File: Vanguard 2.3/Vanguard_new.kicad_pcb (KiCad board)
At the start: 4 copper layers, 42.3 x 51.9 mm, 88 parts, among them J1 USB_C_Receptacle_USB2.0_16P, J2 Conn_02x03_Pin, J3 Micro_SD_Card_Det1, J4 STARBOARD_SERVO, J5 PORTSIDE_SERVO, J6 Battery In, J7 EJECTION_SERVO, Q1 BSS138, Q2 BSS138, Q3 BSS138, Q4 BSS138, U1 ATSAMD11D14A-M, U2 ATmega4809-A, U3 AT25DF641A-SH-T, U4 AP2112K-3.3, U5 BD1020HFV, U6 BNO086, U7 TXB0104D, U8 TPS61092, U9 MPM3610AGQV-P, Y1 32.768kHz

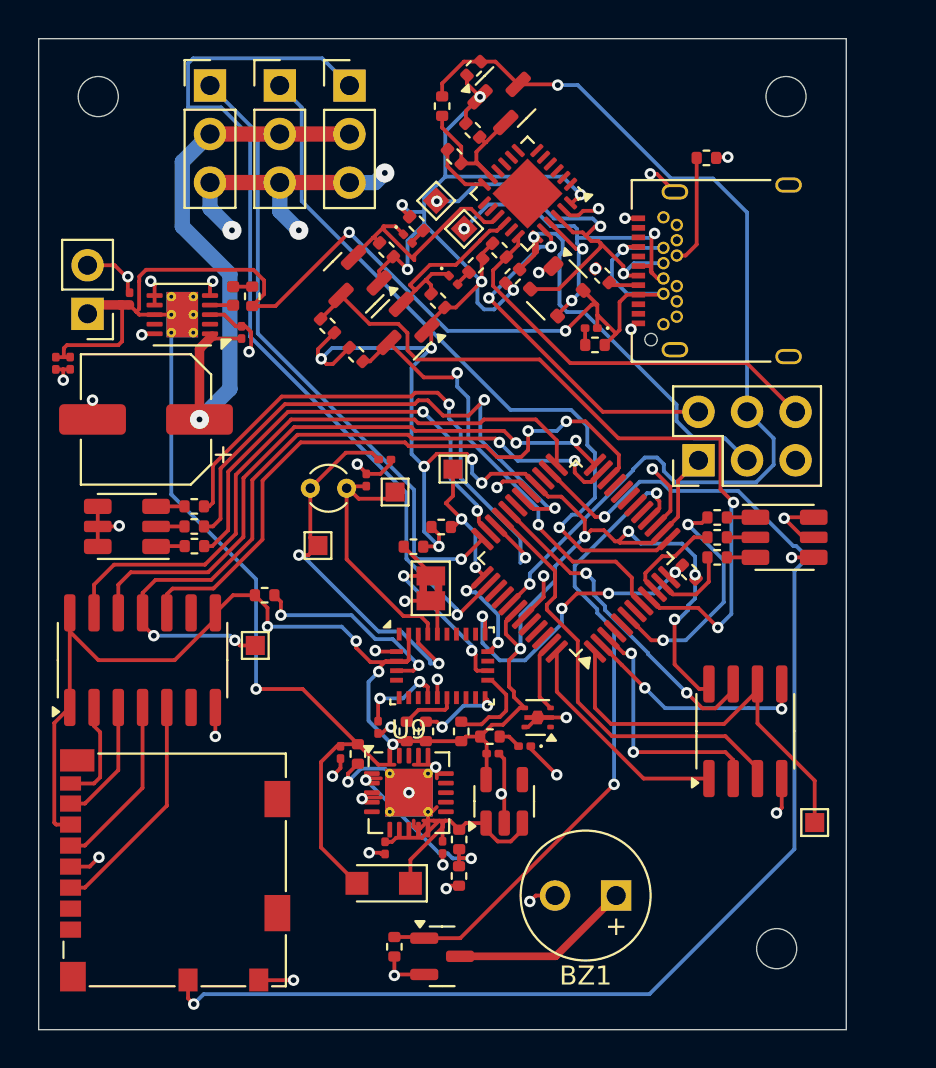
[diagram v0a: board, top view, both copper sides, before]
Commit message: wired u9 + new drc rules
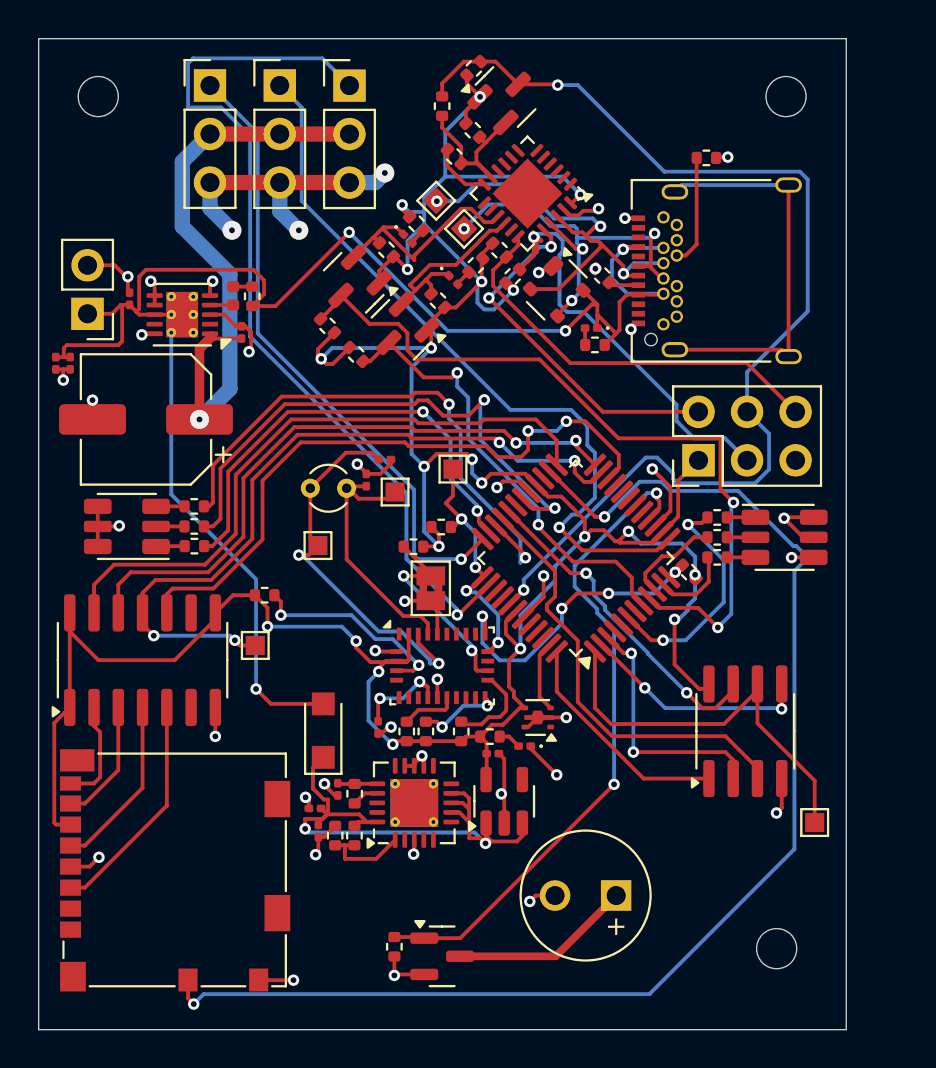
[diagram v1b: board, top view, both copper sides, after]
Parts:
- moved D6 8.59 mm to (107.3, 120.2), turned to 90 degrees
- moved C5 6.98 mm to (106.8, 124.3), turned to 180 degrees
- moved R16 6.82 mm to (107.9, 125.7), turned to 90 degrees
- moved R15 5.49 mm to (108.9, 125.7)
- moved C11 3.60 mm to (107.0, 125.4)
- moved R14 2.09 mm to (108.9, 123.5)
- moved C4 1.94 mm to (108.0, 123.3)
- moved U9 0.61 mm to (112.0, 124.0), turned to 90 degrees
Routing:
- net unconnected-(J1-SHIELD-PadS1): track 1.68 -> 21.2 mm, vias 1 -> 0
- net BATT_IN: track 100.4 -> 85.9 mm
- net Net-(D6-K): track 17.4 -> 30.8 mm, vias 0 -> 2
- net UPDI: track 52.7 -> 57.9 mm
- net Net-(U9-FB): track 9.59 -> 4.77 mm, vias 2 -> 0
- net Net-(U9-EN): track 5.17 -> 1.40 mm, vias 2 -> 0
- net Net-(U9-IN): track 0.00 -> 2.09 mm
- net GND: track 82.5 -> 83.3 mm, vias 42 -> 41

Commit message: fix wiring fixed meddyfix wiring fixed meddyfix wiring fixed meddyfix wiring fixed meddyfix wiring fixed meddyfix wiring fixed meddyfix wiring fixed meddyfix wiring fixed meddyfix wiring fixed meddyfix wiring fixed meddyfix wiring fixed meddyfix wiring fixed meddyfix wiring fixed meddyfix wiring fixed meddyfix wiring fixed meddyfix wiring fixed meddyfix wiring fixed meddyfix wiring fixed meddyfix wiring fixed meddy
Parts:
- moved TP4 10.4 mm to (130.1, 115.0)
- moved REF** 0.81 mm to (131.5, 132.2)
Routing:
- net (no net): track 0.00 -> 96.3 mm
- net GND: track 83.3 -> 69.1 mm, vias 41 -> 38
- net +5V: track 31.0 -> 40.2 mm, vias 1 -> 2
- net PA2/SCK: track 21.4 -> 15.0 mm
- net RX0: track 39.9 -> 37.6 mm
- net STAR_BLUE: track 12.3 -> 10.6 mm
- net +3.3V: track 167.2 -> 165.9 mm
- net BATT_IN: track 85.9 -> 84.7 mm
- net Net-(U6-XOUT32/CLKSEL1): track 13.8 -> 13.0 mm
- net PA0/MISO: track 13.1 -> 12.4 mm
- net D4: track 38.9 -> 38.3 mm
- net Net-(U6-XIN32): track 20.6 -> 20.1 mm

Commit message: i forgot what i did
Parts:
- moved REF** 0.58 mm to (131.4, 132.8)
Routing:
- net GND: track 69.1 -> 66.3 mm

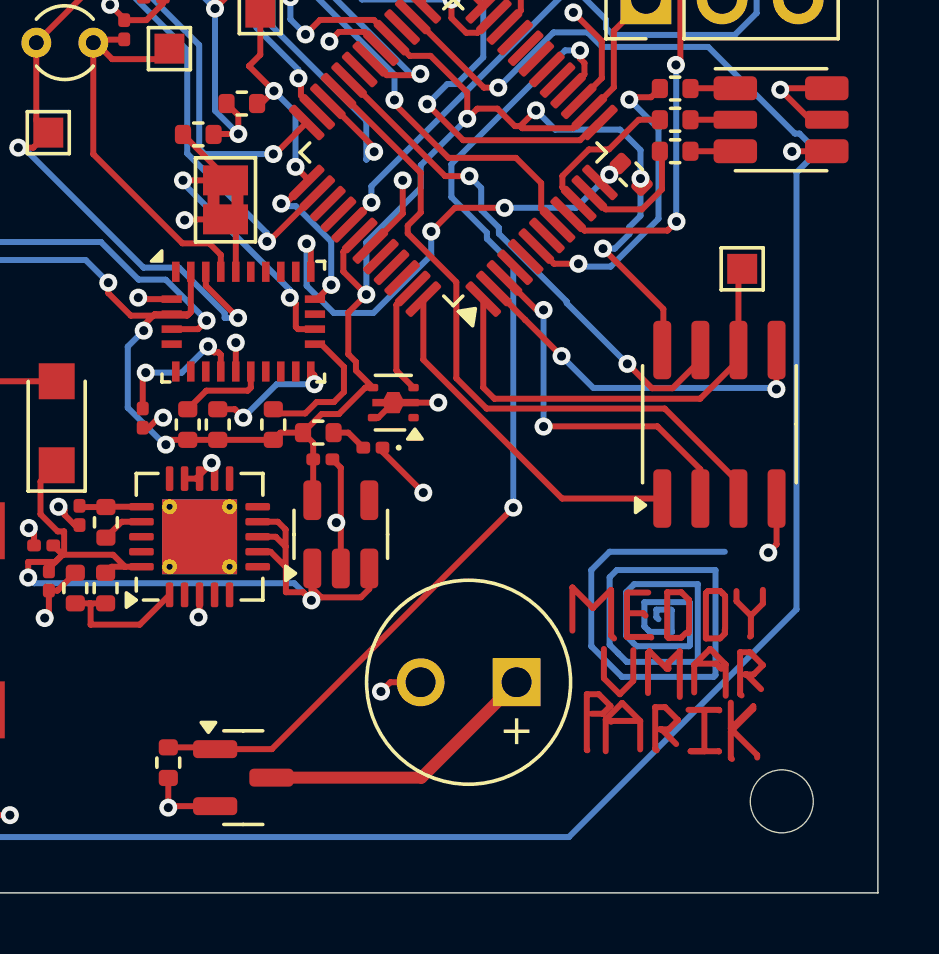
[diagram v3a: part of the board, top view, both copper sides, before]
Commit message: wired mpl370l
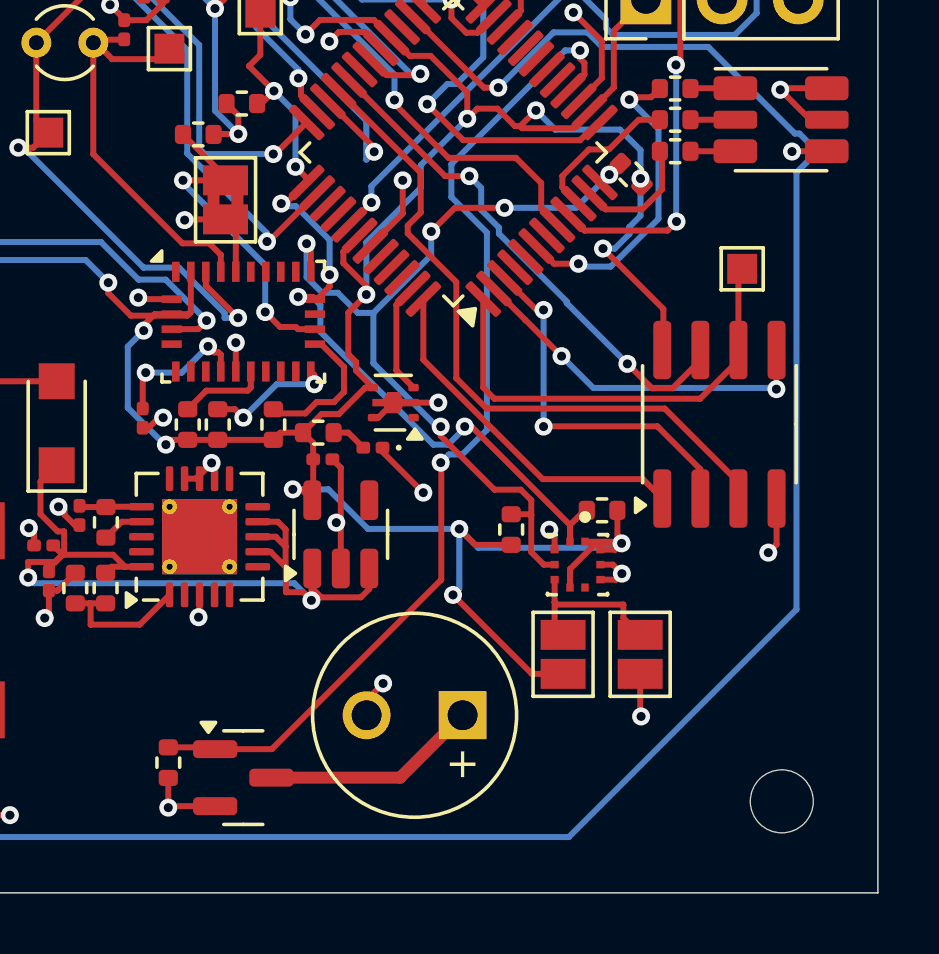
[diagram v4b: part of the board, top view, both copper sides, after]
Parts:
- added JP1: Jumper_2_Small_Open, Jumper:SolderJumper-2_P1.3mm_Open_Pad1.0x1.5mm, F.Cu at (126.7, 127.9)
- added JP2: Jumper_2_Small_Open, Jumper:SolderJumper-2_P1.3mm_Open_Pad1.0x1.5mm, F.Cu at (124.2, 127.9)
- added R1: 4.7kΩ, Resistor_SMD:R_0402_1005Metric, F.Cu at (125.5, 123.1)
- added R36: 4.7kΩ, Resistor_SMD:R_0402_1005Metric, F.Cu at (122.4, 123.7)
- added U10: BMP390L, BMP390L:XDCR_BMP390L, F.Cu at (124.6, 124.9)
- moved BZ1 2.11 mm to (120.8, 129.9)
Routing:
- net (no net): track 96.7 -> 0.00 mm
- net +3.3V: track 165.9 -> 193.4 mm, vias 21 -> 25
- net SCL: track 12.6 -> 27.8 mm, vias 4 -> 6
- net SDA: track 16.1 -> 28.3 mm, vias 4 -> 5
- net Net-(JP1-A): track 0.00 -> 5.52 mm
- net GND: track 66.3 -> 70.0 mm, vias 38 -> 41
- net Net-(BZ1-+): track 9.49 -> 7.23 mm

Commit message: pcb; patrick pls check
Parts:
- J1: footprint Connector_USB:USB_C_Receptacle_Amphenol_12401548E4-2A -> Connector_USB:USB_C_Receptacle_GCT_USB4085
- moved TP1 13.2 mm to (125.4, 97.3), turned to 0 degrees
- moved R32 11.9 mm to (132.0, 101.1)
- moved R35 10.3 mm to (127.0, 91.3), turned to -90 degrees
- moved D7 9.56 mm to (126.1, 90.8), turned to 90 degrees
- moved D1 6.57 mm to (125.1, 93.6), turned to 45 degrees
- moved TP2 6.25 mm to (120.0, 97.1), turned to 0 degrees
- moved R31 5.15 mm to (127.0, 97.2), turned to -90 degrees
- moved J1 2.10 mm to (128.6, 98.2)
- moved C2 0.21 mm to (109.7, 107.2)
- moved TP6 0.07 mm to (111.1, 107.7)
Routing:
- net Net-(D1-I/O1): track 23.7 -> 15.5 mm, vias 3 -> 2
- net UPDI: track 57.9 -> 50.5 mm
- net Net-(D1-I/O2): track 21.9 -> 15.1 mm, vias 4 -> 0
- net unconnected-(J1-SHIELD-PadS1): track 21.2 -> 15.4 mm
- net BATT_IN: track 84.7 -> 88.0 mm, vias 4 -> 3
- net Net-(J1-CC2): track 5.81 -> 8.67 mm, vias 0 -> 1
- net GND: track 70.0 -> 70.9 mm
- net Net-(U6-XOUT32/CLKSEL1): track 13.0 -> 13.9 mm

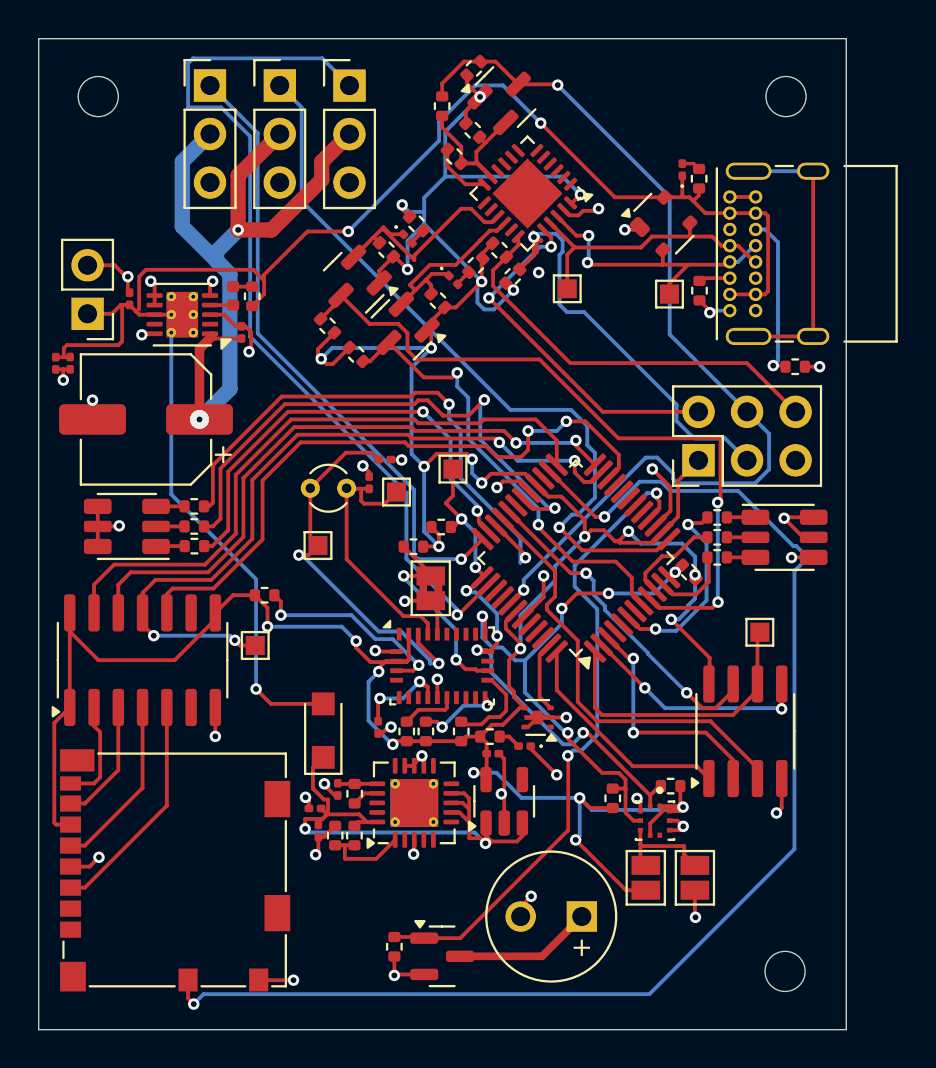
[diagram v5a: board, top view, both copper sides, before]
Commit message: moved crystal + shortened traces
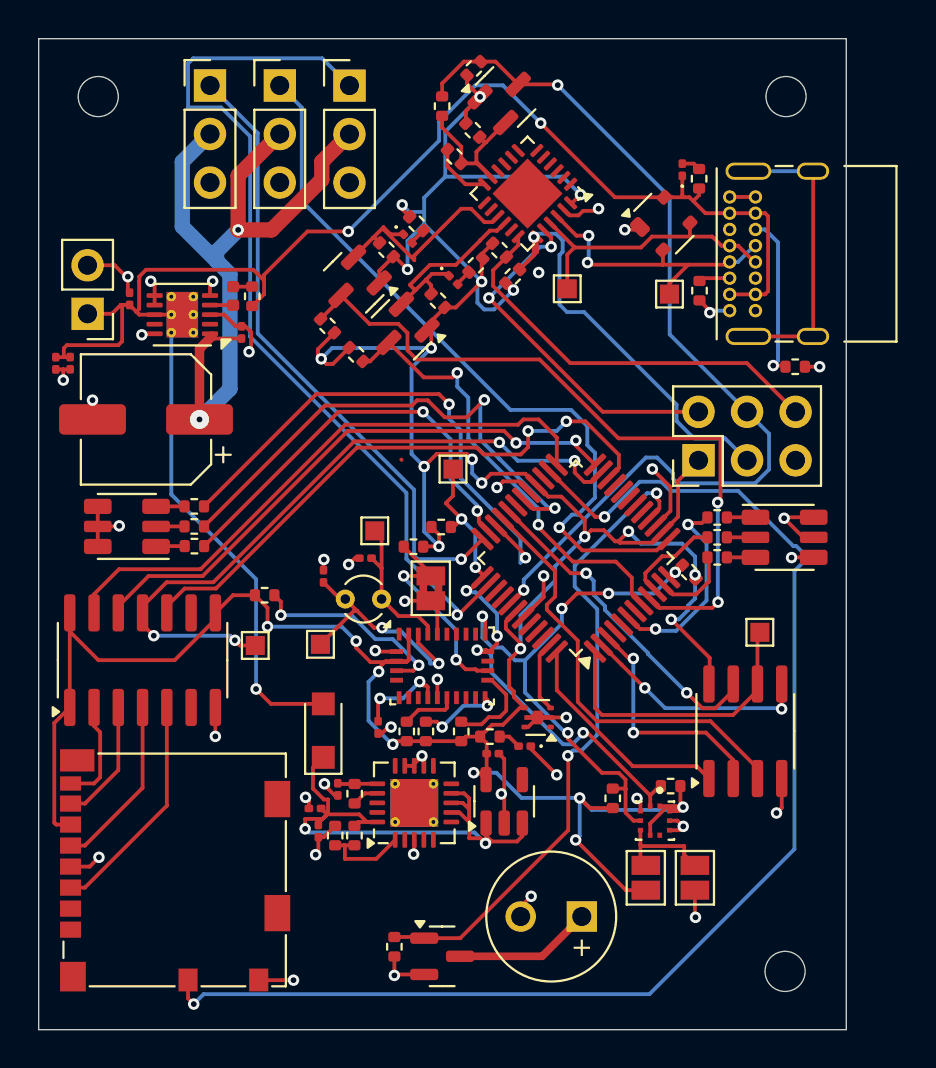
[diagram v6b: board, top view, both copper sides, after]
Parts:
- moved C3 6.90 mm to (107.3, 112.1), turned to 90 degrees
- moved Y1 6.08 mm to (110.3, 113.3)
- moved TP5 5.17 mm to (107.1, 115.7)
- moved C2 3.95 mm to (109.5, 111.2), turned to 180 degrees
- moved TP6 2.33 mm to (110.0, 109.7), turned to 90 degrees
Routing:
- net Net-(U6-XIN32): track 20.1 -> 12.5 mm
- net Net-(U6-XOUT32/CLKSEL1): track 13.9 -> 7.89 mm
- net D6: track 32.7 -> 30.1 mm
- net D5: track 33.6 -> 31.0 mm
- net D4: track 38.3 -> 35.8 mm
- net D7: track 33.0 -> 30.8 mm
- net PORT_BLUE: track 24.0 -> 22.2 mm
- net PORT_RED: track 29.1 -> 27.6 mm
- net PORT_GREEN: track 29.2 -> 28.0 mm
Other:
- outline, holes or cut-outs redrawn

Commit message: jst ph battery connector inserted- closeout ready for 5ver review
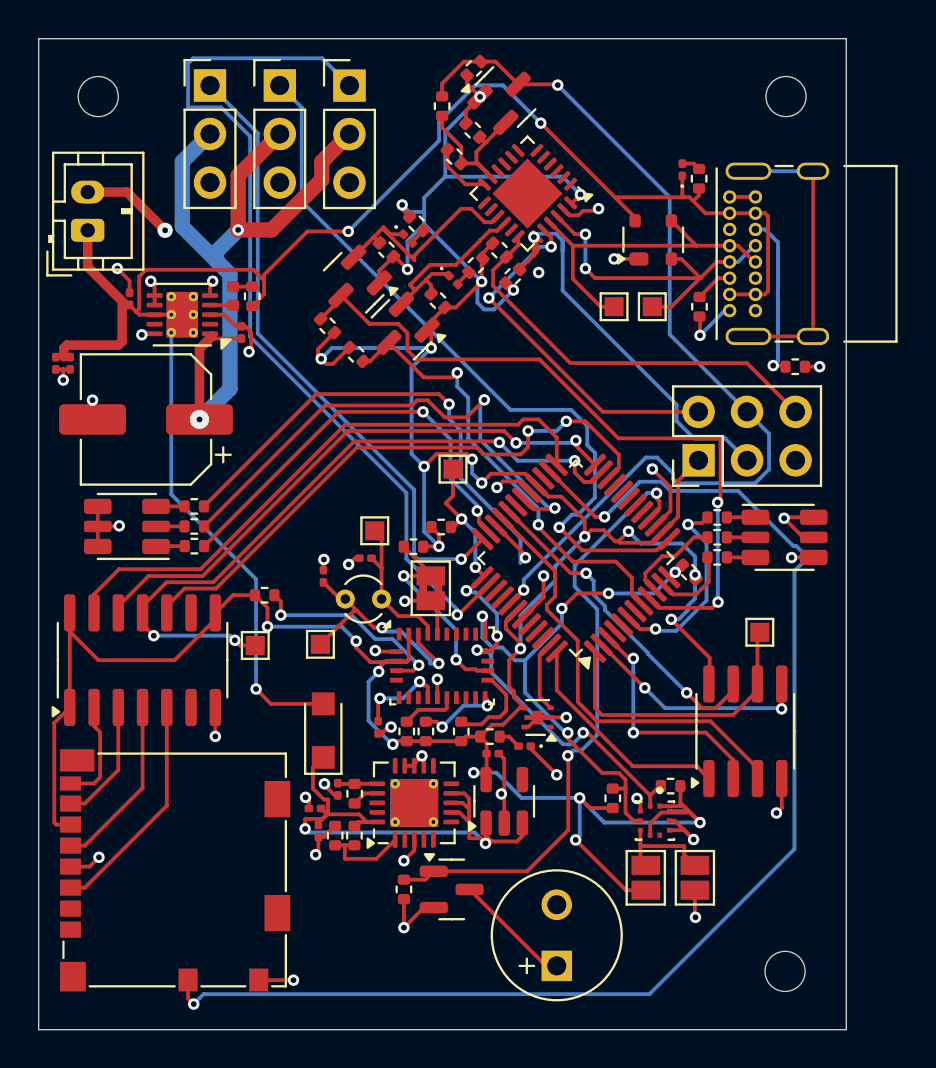
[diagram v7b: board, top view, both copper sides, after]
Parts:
- J6: footprint Connector_PinHeader_2.54mm:PinHeader_1x02_P2.54mm_Vertical -> Connector_JST:JST_PH_B2B-PH-K_1x02_P2.00mm_Vertical
- moved J6 4.37 mm to (95.0, 94.0), turned to 90 degrees
- moved Q4 3.54 mm to (114.0, 128.5)
- moved R34 3.04 mm to (111.5, 128.5)
- moved BZ1 2.89 mm to (119.5, 132.5), turned to 90 degrees
- moved TP2 2.62 mm to (122.5, 98.0)
- moved TP1 1.12 mm to (124.5, 98.0)
- moved D1 1.01 mm to (124.5, 94.5), turned to 90 degrees
- moved R31 0.84 mm to (127.0, 98.0)
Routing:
- net GND: track 70.9 -> 77.9 mm
- net +3.3V: track 193.4 -> 198.9 mm
- net BATT_IN: track 88.0 -> 92.7 mm
- net Net-(D1-I/O1): track 15.5 -> 18.5 mm
- net Net-(D1-I/O2): track 15.1 -> 17.9 mm
- net BUZZER: track 34.1 -> 32.4 mm
- net Net-(BZ1-+): track 7.23 -> 6.22 mm
